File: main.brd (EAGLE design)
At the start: 16.5 x 35.5 mm, 18 parts, among them IC1 TINY45/85, U1 TMP102, X1 MINI-USB-UX60-MB-5ST

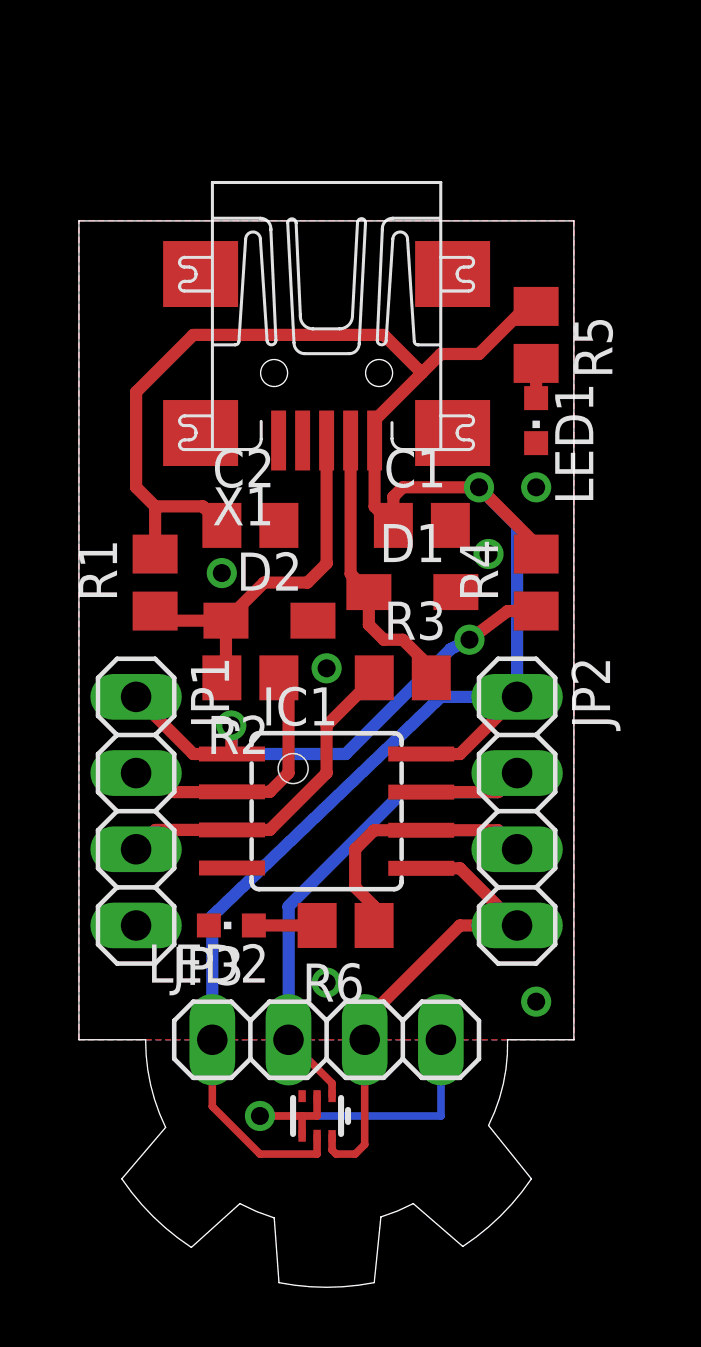
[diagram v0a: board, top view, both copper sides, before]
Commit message: Added EARS Logo
Added EARS logo to the underside of the PCB. Used a scale factor of
0.75
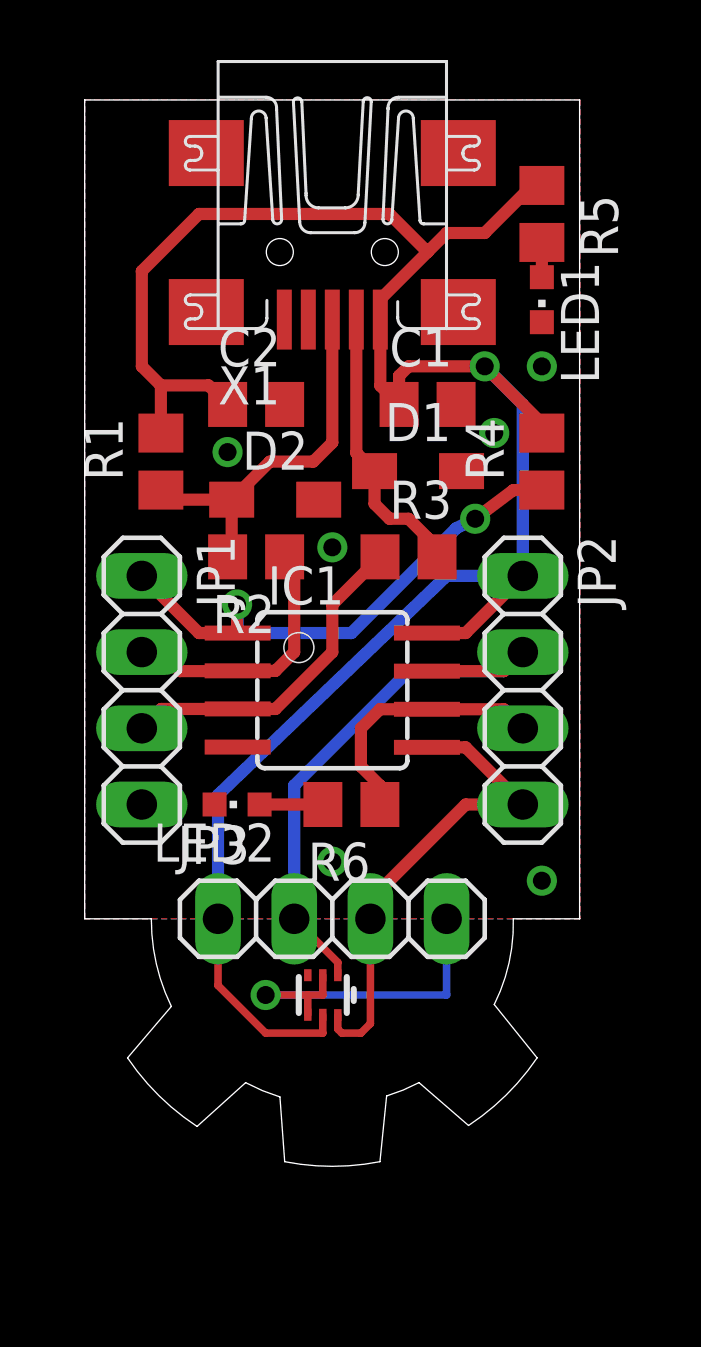
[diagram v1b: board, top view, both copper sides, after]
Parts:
- moved C1 4.04 mm to (11.6, 25.6)
- moved C2 4.04 mm to (5.91, 25.6)
- moved D1 4.04 mm to (11.3, 23.4)
- moved D2 4.04 mm to (6.54, 22.4)
- moved LED1 4.04 mm to (15.4, 29.1)
- moved R1 4.04 mm to (2.73, 23.7)
- moved R4 4.04 mm to (15.4, 23.7)
- moved IC1 4.04 mm to (8.45, 16.1)
- moved JP1 4.04 mm to (2.10, 16.1)
- moved JP2 4.04 mm to (14.8, 16.1)
- moved JP3 4.04 mm to (8.45, 8.48)
- moved LED2 4.04 mm to (5.27, 12.3)
- moved R6 4.04 mm to (9.08, 12.3)
- moved U1 4.04 mm to (8.13, 5.94)
- moved R2 4.04 mm to (5.91, 20.5)
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
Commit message: Replaced USB socket
replace USB socket with the 10033526-N3212MLF as per:
http://goodfet.sourceforge.net/hardware/facedancer20/
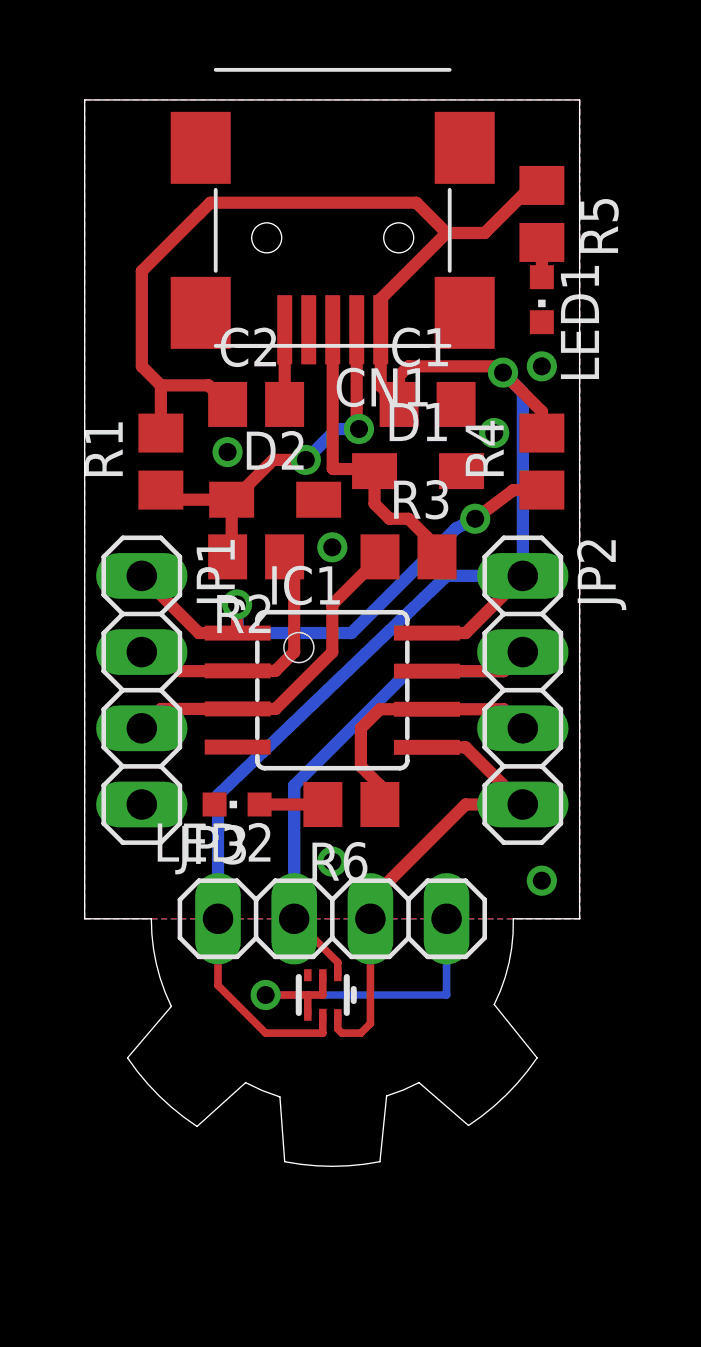
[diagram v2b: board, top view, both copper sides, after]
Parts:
- removed X1: MINI-USB-UX60-MB-5ST, con-hirose:UX60-MB-5ST
- added CN1: (no value), adafruit:USB-MINIB
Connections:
- net +5V: now also CN1.VBUS; no longer X1.1
- net GND: now also CN1.GND; no longer X1.5
- net N$10: now also CN1.D+; no longer X1.2
- net N$8: now also CN1.D-; no longer X1.3
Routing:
- net GND: track 11.8 -> 14.3 mm
- net N$10: track 9.40 -> 10.1 mm
- net N$8: track 12.7 -> 13.0 mm, vias 0 -> 2

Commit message: changed sensor. sorted silk.
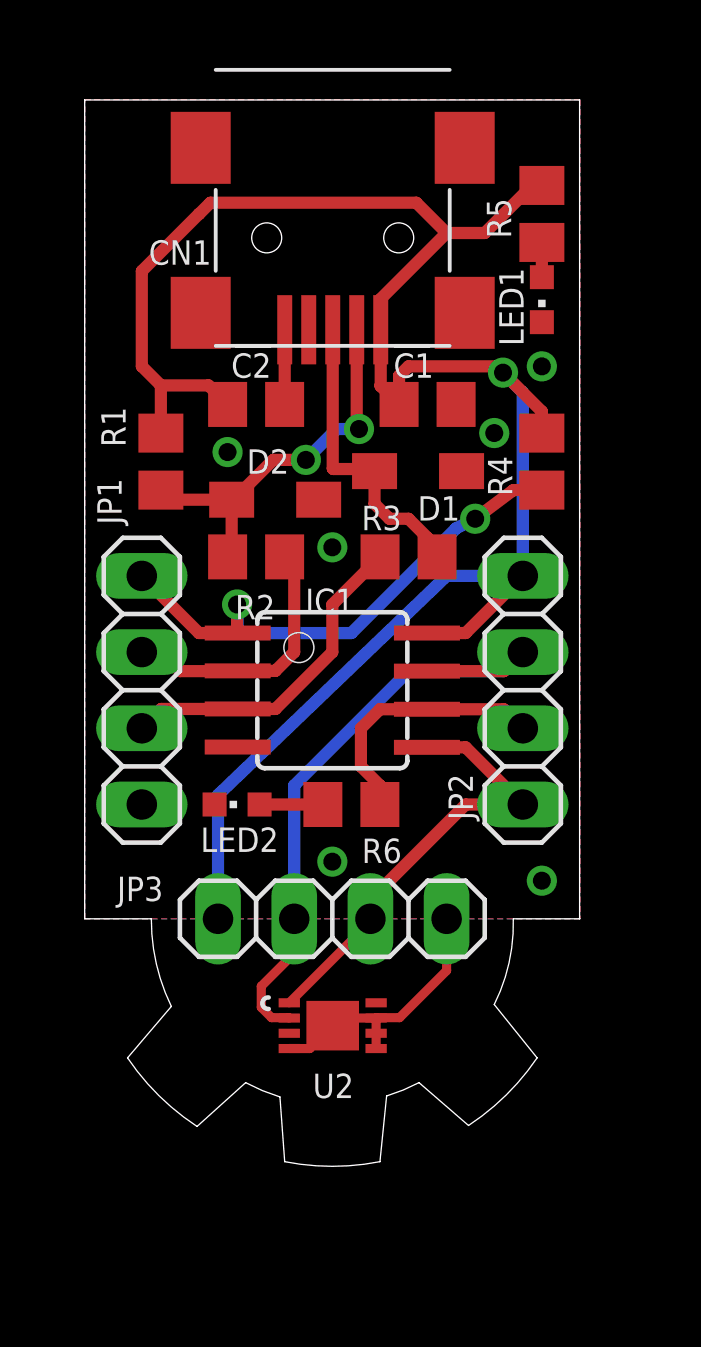
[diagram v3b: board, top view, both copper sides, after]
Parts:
- removed U1: TMP102, SparkFun-Sensors:SOT563
- added U2: (no value), mattsLib:DFN300X200X100-9N
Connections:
- new net VDD: U2.8
- net +5V: no longer U1.5
- net GND: now also U2.4, U2.5, U2.6, U2.7, U2.9; no longer U1.2, U1.4
- net N$5: now also U2.2; no longer U1.1
- net N$9: now also U2.1; no longer U1.6
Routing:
- net +5V: track 72.8 -> 65.9 mm
- net GND: track 14.3 -> 11.6 mm, vias 7 -> 6
- net N$5: track 19.8 -> 21.9 mm
- net N$9: track 16.2 -> 14.9 mm

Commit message: Shifted some silk, down the bazaar like. Added via to allow ground plane between I2C lines. Added gerbers.
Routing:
- net GND: vias 6 -> 7
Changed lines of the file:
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@@
 </element>
 <element name="LED2" library="led" package="CHIPLED_0603" value="" x="5.2705" y="12.28725" smashed="yes" rot="R90">
-<attribute name="NAME" x="6.6548" y="11.5189" size="0.8128" layer="25" rot="R180"/>
+<attribute name="NAME" x="6.8072" y="11.69035" size="0.8128" layer="25" rot="R180"/>
 <attribute name="VALUE" x="6.5405" y="14.19225" size="1.27" layer="27" rot="R180"/>
 </element>
@@
 <wire x1="9.906" y1="5.1689" x2="8.7122" y2="5.1689" width="0.3048" layer="1"/>
 <wire x1="8.7122" y1="5.1689" x2="8.4582" y2="4.9149" width="0.3048" layer="1"/>
+<via x="5.9055" y="10.4013" extent="1-16" drill="0.6" shape="octagon"/>
+<wire x1="4.5205" y1="12.28725" x2="5.9055" y2="10.4013" width="0" layer="19" extent="1-1"/>
 </signal>
 <signal name="N$1">

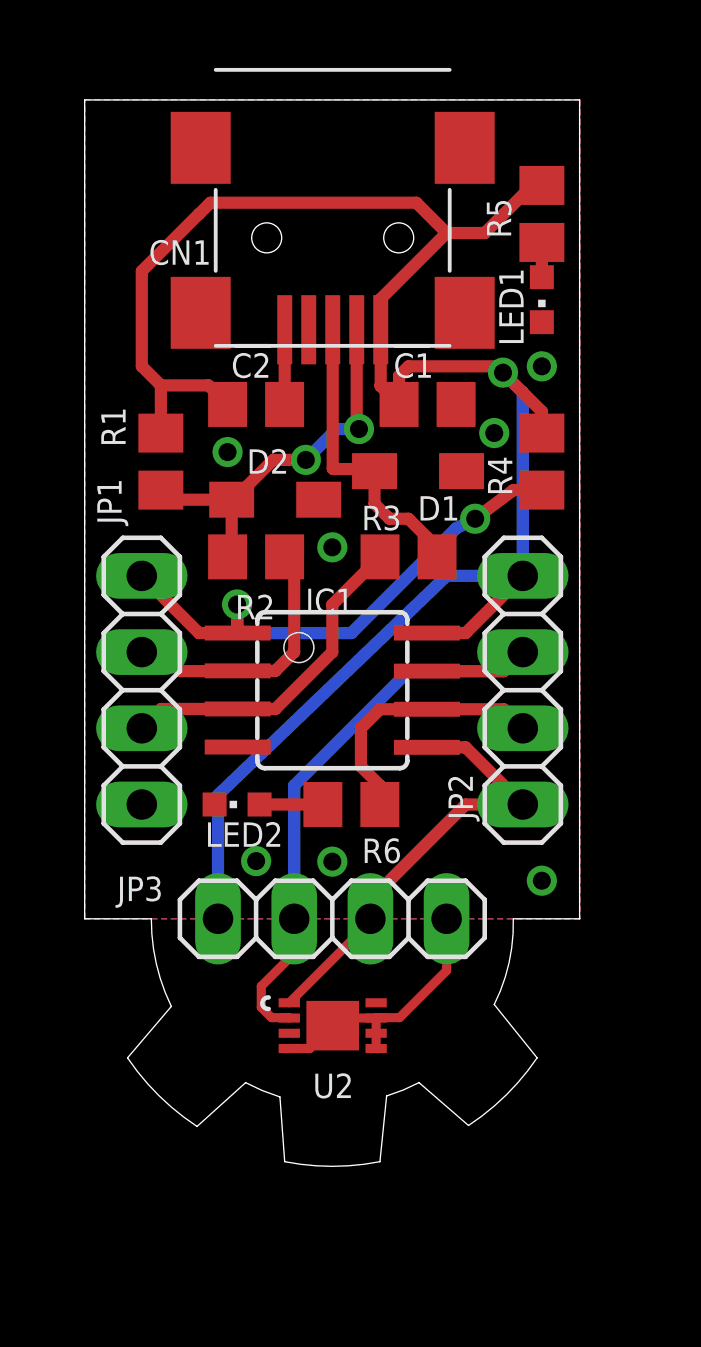
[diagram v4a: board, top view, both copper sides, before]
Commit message: Fixed text, added pull ups.
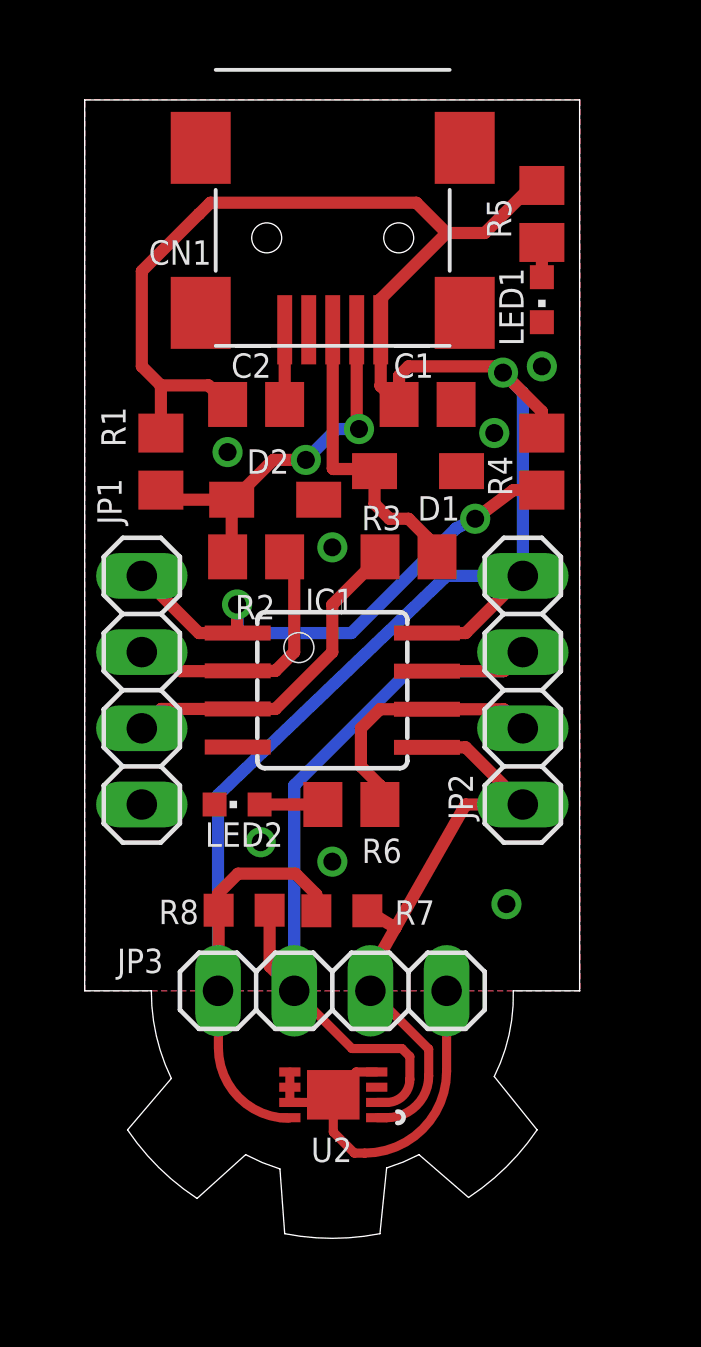
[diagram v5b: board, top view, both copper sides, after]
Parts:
- added R7, R8: 10k, resistor:R0603
- moved JP3 2.40 mm to (8.45, 6.08)
- moved U2 2.31 mm to (8.48, 2.61), turned to 180 degrees
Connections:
- net +5V: now also R7.2, R8.2
- net N$5: now also R8.1
- net N$9: now also R7.1
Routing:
- net +5V: track 65.9 -> 75.9 mm
- net N$5: track 21.9 -> 29.7 mm
- net N$11: track 0.00 -> 5.16 mm
- net N$9: track 14.9 -> 20.1 mm
- net GND: track 11.6 -> 15.9 mm
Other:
- board size 16.5 x 35.5 mm -> 16.5 x 37.9 mm

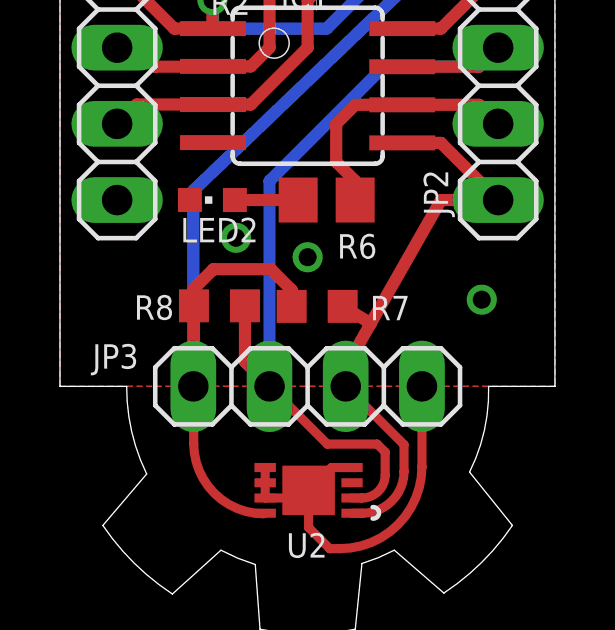
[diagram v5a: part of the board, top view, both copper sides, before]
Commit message: Pulled BoM.xlsx, also changed pull ups to 0805
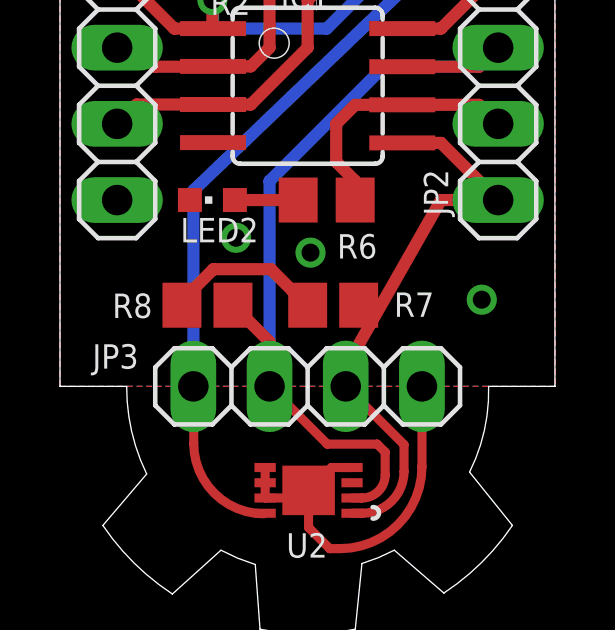
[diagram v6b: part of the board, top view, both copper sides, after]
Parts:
- R7, R8: device resistor:R0603 -> resistor:R0805
- moved R7 0.53 mm to (9.30, 8.78)
- moved R8 0.40 mm to (5.11, 8.78)
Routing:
- net +5V: track 75.9 -> 73.8 mm
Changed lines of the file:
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@@
 <attribute name="VALUE" x="14.19225" y="6.08965" size="2.0828" layer="27" ratio="10" rot="SR180"/>
 </element>
-<element name="R7" library="resistor" package="R0603" value="10k" x="8.763" y="8.74395" smashed="yes" rot="R180">
-<attribute name="NAME" x="11.8618" y="9.0932" size="0.8128" layer="25" rot="R180"/>
+<element name="R7" library="resistor" package="R0805" value="10k" x="9.2964" y="8.78205" smashed="yes" rot="R180">
+<attribute name="NAME" x="12.6619" y="9.2075" size="0.8128" layer="25" rot="R180"/>
 </element>
-<element name="R8" library="resistor" package="R0603" value="10k" x="5.50545" y="8.763" smashed="yes" rot="R180">
-<attribute name="NAME" x="3.99415" y="9.11225" size="0.8128" layer="25" rot="R180"/>
+<element name="R8" library="resistor" package="R0805" value="10k" x="5.1054" y="8.78205" smashed="yes" rot="R180">
+<attribute name="NAME" x="3.27025" y="9.1694" size="0.8128" layer="25" rot="R180"/>
 </element>
 </elements>
@@
 <via x="13.843" y="24.66975" extent="1-16" drill="0.6" shape="octagon"/>
 <via x="14.2494" y="8.9662" extent="1-16" drill="0.6" shape="octagon"/>
-<via x="8.4455" y="10.38225" extent="1-16" drill="0.6" shape="octagon"/>
+<via x="8.54075" y="10.53465" extent="1-16" drill="0.6" shape="octagon"/>
 <contactref element="CN1" pad="GND"/>
 <wire x1="6.8582" y1="28.11145" x2="6.8582" y2="25.62495" width="0.4064" layer="1"/>
@@
 <wire x1="9.7155" y1="6.07695" x2="9.7155" y2="5.9817" width="0.3048" layer="1"/>
 <contactref element="R7" pad="1"/>
-<wire x1="9.613" y1="8.74395" x2="10.549609375" y2="8.176646875" width="0.4064" layer="1"/>
+<wire x1="10.1464" y1="8.78205" x2="10.549609375" y2="8.176646875" width="0.4064" layer="1"/>
 <wire x1="9.92505" y1="1.84785" x2="10.26795" y2="1.84785" width="0.3048" layer="1"/>
 <wire x1="10.26795" y1="1.84785" x2="11.6586" y2="3.2385" width="0.3048" layer="1" curve="90"/>
@@
 <contactref element="R7" pad="2"/>
 <contactref element="R8" pad="2"/>
-<wire x1="4.65545" y1="8.763" x2="4.65545" y2="6.0969" width="0.4064" layer="1"/>
 <wire x1="4.65545" y1="6.0969" x2="4.6355" y2="6.07695" width="0.4064" layer="1" curve="-90"/>
-<wire x1="7.913" y1="8.74395" x2="7.913" y2="9.28915" width="0.4064" layer="1"/>
+<wire x1="8.4464" y1="8.78205" x2="7.913" y2="9.28915" width="0.4064" layer="1"/>
 <wire x1="7.913" y1="9.28915" x2="7.21995" y2="9.9822" width="0.4064" layer="1"/>
 <wire x1="7.21995" y1="9.9822" x2="5.30225" y2="9.9822" width="0.4064" layer="1"/>
 <wire x1="5.30225" y1="9.9822" x2="4.6355" y2="9.31545" width="0.4064" layer="1"/>
 <wire x1="4.6355" y1="9.31545" x2="4.6355" y2="8.78295" width="0.4064" layer="1"/>
-<wire x1="4.6355" y1="8.78295" x2="4.65545" y2="8.763" width="0.4064" layer="1"/>
+<wire x1="4.6355" y1="8.78295" x2="4.2554" y2="8.78205" width="0.4064" layer="1"/>
+<wire x1="4.65545" y1="6.0969" x2="4.6355" y2="8.78295" width="0" layer="19" extent="1-1"/>
 </signal>
 <signal name="N$5">
@@
 <contactref element="U2" pad="2"/>
 <contactref element="R8" pad="1"/>
-<wire x1="6.35545" y1="8.763" x2="6.35545" y2="6.897" width="0.4064" layer="1"/>
-<wire x1="6.35545" y1="6.897" x2="7.1755" y2="6.07695" width="0.4064" layer="1"/>
 <wire x1="9.92505" y1="2.35585" x2="10.2616" y2="2.35585" width="0.3048" layer="1"/>
 <wire x1="10.2616" y1="2.35585" x2="11.02995" y2="3.1242" width="0.3048" layer="1" curve="90"/>
@@
 <wire x1="10.76325" y1="4.1529" x2="9.09955" y2="4.1529" width="0.3048" layer="1"/>
 <wire x1="9.09955" y1="4.1529" x2="7.1755" y2="6.07695" width="0.3048" layer="1"/>
+<wire x1="5.9554" y1="8.78205" x2="7.1755" y2="7.56195" width="0.4064" layer="1"/>
+<wire x1="7.1755" y1="7.56195" x2="7.1755" y2="6.07695" width="0.4064" layer="1"/>
 </signal>
 <signal name="N$2">
